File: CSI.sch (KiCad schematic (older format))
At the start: 1 part, among them U1 MIMX8MM6DVTLZAA

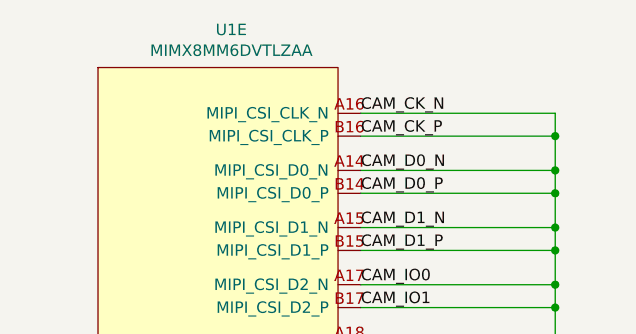
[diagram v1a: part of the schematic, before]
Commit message: Complete entry of bom
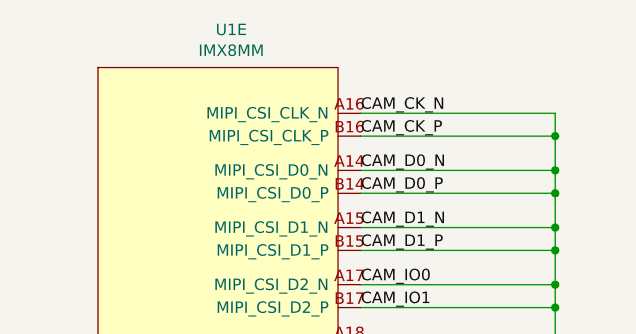
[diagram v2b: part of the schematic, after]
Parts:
- U1: value MIMX8MM6DVTLZAA -> IMX8MM; Mfgr (none) -> NXP; Part (none) -> MIMX8MM6CVTKZAA; Vendorpart (none) -> 568-15276-ND
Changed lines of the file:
@@
 P 3750 6200
 F 0 "U1" H 3783 9065 50  0000 C CNN
-F 1 "MIMX8MM6DVTLZAA" H 3783 8974 50  0000 C CNN
+F 1 "IMX8MM" H 3783 8974 50  0000 C CNN
 F 2 "mxenc:BGA-729_27x27_14.0x14.0mm" H 4000 8950 50  0001 C CNN
 F 3 "" H 3000 8950 50  0001 C CNN
+F 4 "NXP" H 3750 6200 50  0001 C CNN "Mfgr"
+F 5 "MIMX8MM6CVTKZAA" H 3750 6200 50  0001 C CNN "Part"
+F 6 "568-15276-ND" H 3750 6200 50  0001 C CNN "Vendorpart"
 	5    3750 6200
 	1    0    0    -1

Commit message: wip more new layout
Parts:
- removed U1: IMX8MM, mxenc:BGA-729_27x27_14.0x14.0mm, symbol mxenc:MIMX8MM6DVTLZAA
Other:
- note removed: "i.MX8MM HDG Unused signal strapping\nMIPI-CSI - MIPI_CSI_CLK_P/N, MIPI_CSI_Dx_P/N - Tie all signals to ground"
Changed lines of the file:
@@
 $Descr A4 11693 8268
 encoding utf-8
-Sheet 8 9
+Sheet 8 10
 Title ""
 Date ""
@@
 Comment4 ""
 $EndDescr
-Text Label 4350 3700 0    50   ~ 0
-CAM_CK_N
-Text Label 4350 3800 0    50   ~ 0
-CAM_CK_P
-Text Label 4350 3950 0    50   ~ 0
-CAM_D0_N
-Text Label 4350 4050 0    50   ~ 0
-CAM_D0_P
-Text Label 4350 4200 0    50   ~ 0
-CAM_D1_N
-Text Label 4350 4300 0    50   ~ 0
-CAM_D1_P
-Text Label 4350 4450 0    50   ~ 0
-CAM_IO0
-Text Label 4350 4550 0    50   ~ 0
-CAM_IO1
-$Comp
-L power:GND #PWR0245
-U 1 1 5D5D8BBA
-P 5200 4850
-F 0 "#PWR0245" H 5200 4600 50  0001 C CNN
-F 1 "GND" H 5205 4677 50  0000 C CNN
-F 2 "" H 5200 4850 50  0001 C CNN
-F 3 "" H 5200 4850 50  0001 C CNN
-	1    5200 4850
-	1    0    0    -1
-$EndComp
-Wire Wire Line
-	5200 4850 5200 4800
-Wire Wire Line
-	5200 4550 4350 4550
-Wire Wire Line
-	5200 3700 4350 3700
-Connection ~ 5200 4550
-Wire Wire Line
-	4350 3800 5200 3800
-Connection ~ 5200 3800
-Wire Wire Line
-	5200 3800 5200 3700
-Wire Wire Line
-	4350 3950 5200 3950
-Connection ~ 5200 3950
-Wire Wire Line
-	5200 3950 5200 3800
-Wire Wire Line
-	4350 4050 5200 4050
-Connection ~ 5200 4050
-Wire Wire Line
-	5200 4050 5200 3950
-Wire Wire Line
-	4350 4200 5200 4200
-Connection ~ 5200 4200
-Wire Wire Line
-	5200 4200 5200 4050
-Wire Wire Line
-	4350 4300 5200 4300
-Connection ~ 5200 4300
-Wire Wire Line
-	5200 4300 5200 4200
-Wire Wire Line
-	4350 4450 5200 4450
-Wire Wire Line
-	5200 4300 5200 4450
-Connection ~ 5200 4450
-Wire Wire Line
-	5200 4450 5200 4550
-$Comp
-L mxenc:MIMX8MM6DVTLZAA U1
-U 5 1 5DFAB501
-P 3750 6200
-F 0 "U1" H 3783 9065 50  0000 C CNN
-F 1 "IMX8MM" H 3783 8974 50  0000 C CNN
-F 2 "mxenc:BGA-729_27x27_14.0x14.0mm" H 4000 8950 50  0001 C CNN
-F 3 "" H 3000 8950 50  0001 C CNN
-F 4 "NXP" H 3750 6200 50  0001 C CNN "Mfgr"
-F 5 "MIMX8MM6CVTKZAA" H 3750 6200 50  0001 C CNN "Part"
-F 6 "568-15276-ND" H 3750 6200 50  0001 C CNN "Vendorpart"
-	5    3750 6200
-	1    0    0    -1
-$EndComp
-Wire Wire Line
-	4350 4700 5200 4700
-Connection ~ 5200 4700
-Wire Wire Line
-	5200 4700 5200 4550
-Wire Wire Line
-	5200 4700 5200 4800
-Connection ~ 5200 4800
-Wire Wire Line
-	4350 4800 5200 4800
-Text Notes 2850 5550 0    50   ~ 0
-i.MX8MM HDG Unused signal strapping\nMIPI-CSI - MIPI_CSI_CLK_P/N, MIPI_CSI_Dx_P/N - Tie all signals to ground
 $EndSCHEMATC
